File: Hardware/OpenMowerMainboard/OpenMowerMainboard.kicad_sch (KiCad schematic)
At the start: 9 parts, among them U1 LM2596S_MODULE

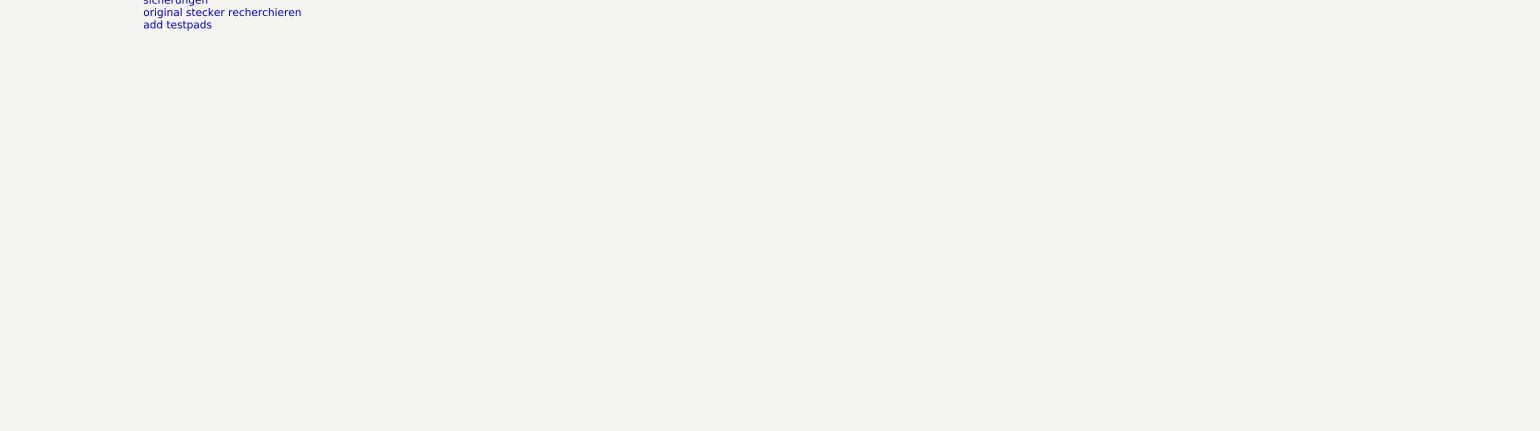
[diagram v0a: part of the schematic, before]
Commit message: added todos, added image of current mainboard
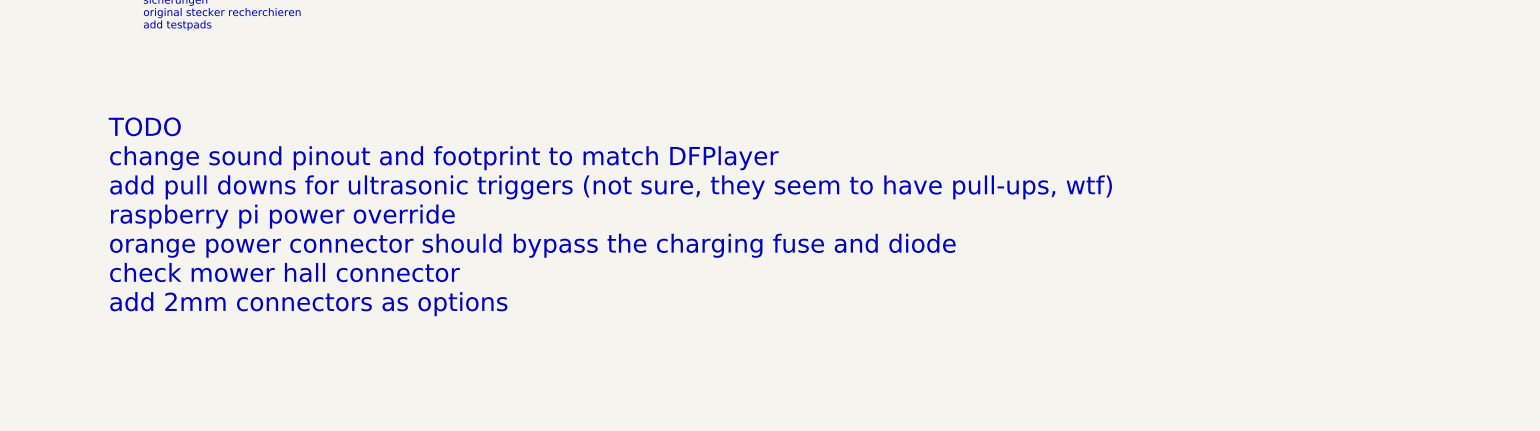
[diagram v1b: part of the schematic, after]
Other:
- note added: "TODO change sound pinout and footprint to match DFPlayer add pull downs for ultrasonic triggers (not sure, they seem to have pull-ups, wtf) raspberry pi power override orange power connector should bypass the charging fuse and diode check mower hall connector add 2mm connectors as options"
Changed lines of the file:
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@@
     (stroke (width 0) (type default) (color 0 0 0 0))
+  )
+  (text "TODO\nchange sound pinout and footprint to match DFPlayer\nadd pull downs for ultrasonic triggers (not sure, they seem to have pull-ups, wtf)\nraspberry pi power override\norange power connector should bypass the charging fuse and diode\ncheck mower hall connector\nadd 2mm connectors as options"
+    (at 282.575 113.665 0)
+    (effects (font (size 3 3)) (justify left bottom))
   )
   (text "Sensor Connectors" (at 50.165 166.37 0)

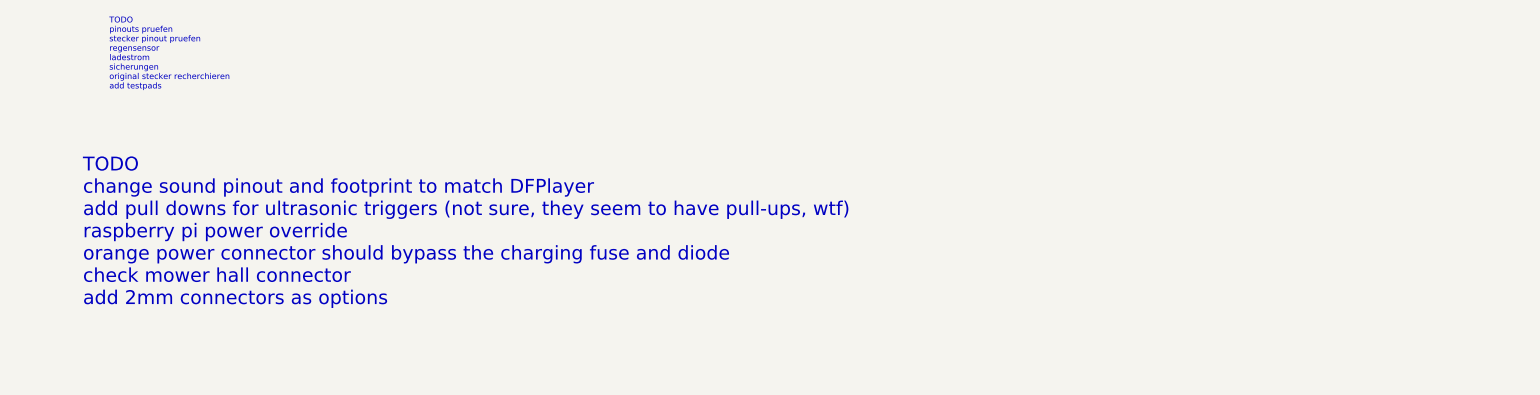
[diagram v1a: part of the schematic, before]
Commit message: Added default pull down, raspberry pi power override and some TODOs
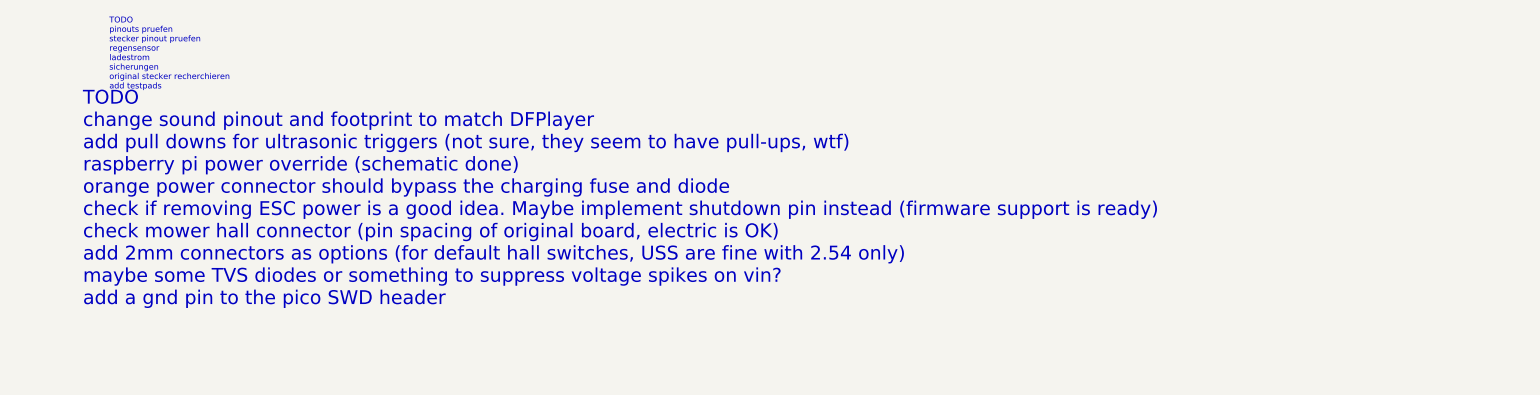
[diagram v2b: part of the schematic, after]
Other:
- note added: "TODO change sound pinout and footprint to match DFPlayer add pull downs for ultrasonic triggers (not sure, they seem to have pull-ups, wtf) raspberry pi power override (schematic done) orange power connector should bypass the charging fuse and diode check if removing ESC power is a good idea. Maybe implement shutdown pin instead (firmware support is ready) check mower hall connector (pin spacing 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"
- note removed: "TODO change sound pinout and footprint to match DFPlayer add pull downs for ultrasonic triggers (not sure, they seem to have pull-ups, wtf) raspberry pi power override orange power connector should bypass the charging fuse and diode check mower hall connector add 2mm connectors as options"
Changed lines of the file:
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@@
     (stroke (width 0) (type default) (color 0 0 0 0))
   )
-  (text "TODO\nchange sound pinout and footprint to match DFPlayer\nadd pull downs for ultrasonic triggers (not sure, they seem to have pull-ups, wtf)\nraspberry pi power override\norange power connector should bypass the charging fuse and diode\ncheck mower hall connector\nadd 2mm connectors as options"
+  (text "TODO\nchange sound pinout and footprint to match DFPlayer\nadd pull downs for ultrasonic triggers (not sure, they seem to have pull-ups, wtf)\nraspberry pi power override (schematic done)\norange power connector should bypass the charging fuse and diode\ncheck if removing ESC power is a good idea. Maybe implement shutdown pin instead (firmware support is ready)\ncheck mower hall connector (pin spacing of original board, electric is OK)\nadd 2mm connectors as options (for default hall switches, USS are fine with 2.54 only)\nmaybe some TVS diodes or something to suppress voltage spikes on vin?\nadd a gnd pin to the pico SWD header"
     (at 282.575 113.665 0)
     (effects (font (size 3 3)) (justify left bottom))
@@
       (reference "R51") (unit 1) (value "R") (footprint "Resistor_SMD:R_2512_6332Metric_Pad1.40x3.35mm_HandSolder")
     )
+    (path "/00000000-0000-0000-0000-00006109dce5/1e0378df-4eb5-4433-998b-5f346ec4a88e"
+      (reference "R?") (unit 1) (value "10k") (footprint "Resistor_SMD:R_0805_2012Metric_Pad1.20x1.40mm_HandSolder")
+    )
+    (path "/00000000-0000-0000-0000-000061080954/524cc440-f69b-4e5c-95c8-45fc44a5eb8a"
+      (reference "R?") (unit 1) (value "10k") (footprint "Resistor_SMD:R_0805_2012Metric_Pad1.20x1.40mm_HandSolder")
+    )
+    (path "/00000000-0000-0000-0000-000061080954/faeb18f8-c222-4c98-a19d-ced7efa28a99"
+      (reference "R?") (unit 1) (value "10k") (footprint "Resistor_SMD:R_0805_2012Metric_Pad1.20x1.40mm_HandSolder")
+    )
     (path "/989a400d-9ce2-403e-a19e-ad0a758fe27c/88528529-64b3-4d79-b2db-e04c4b468443"

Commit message: WIP hardware revision
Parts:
- removed U1: LM2596S_MODULE, MyModules:LM2596S_MODULE, symbol MyModules:LM2596S_MODULE
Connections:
- net V_BATT renamed RobotConnectors/V_BATTERY
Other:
- added sheet dcdc (dcdc.kicad_sch)
- sheet ESCs ports: added none; removed MC_POWER, ML_POWER, MR_POWER
- sheet GPS ports: added none; removed POWER_EN
- sheet RobotConnectors ports: added Enable_Charge, V_BATTERY; removed none
- sheet pico ports: added ENABLE_CHARGE; removed ESC_POWER, GPS_POWER
- note removed: "TODO change sound pinout and footprint to match DFPlayer add pull downs for ultrasonic triggers (not sure, they seem to have pull-ups, wtf) raspberry pi power override (schematic done) orange power connector should bypass the charging fuse and diode check if removing ESC power is a good idea. Maybe implement shutdown pin instead (firmware support is ready) check mower hall connector (pin spacing 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"
- note removed: "TODO pinouts pruefen stecker pinout pruefen regensensor ladestrom sicherungen original stecker recherchieren add testpads"

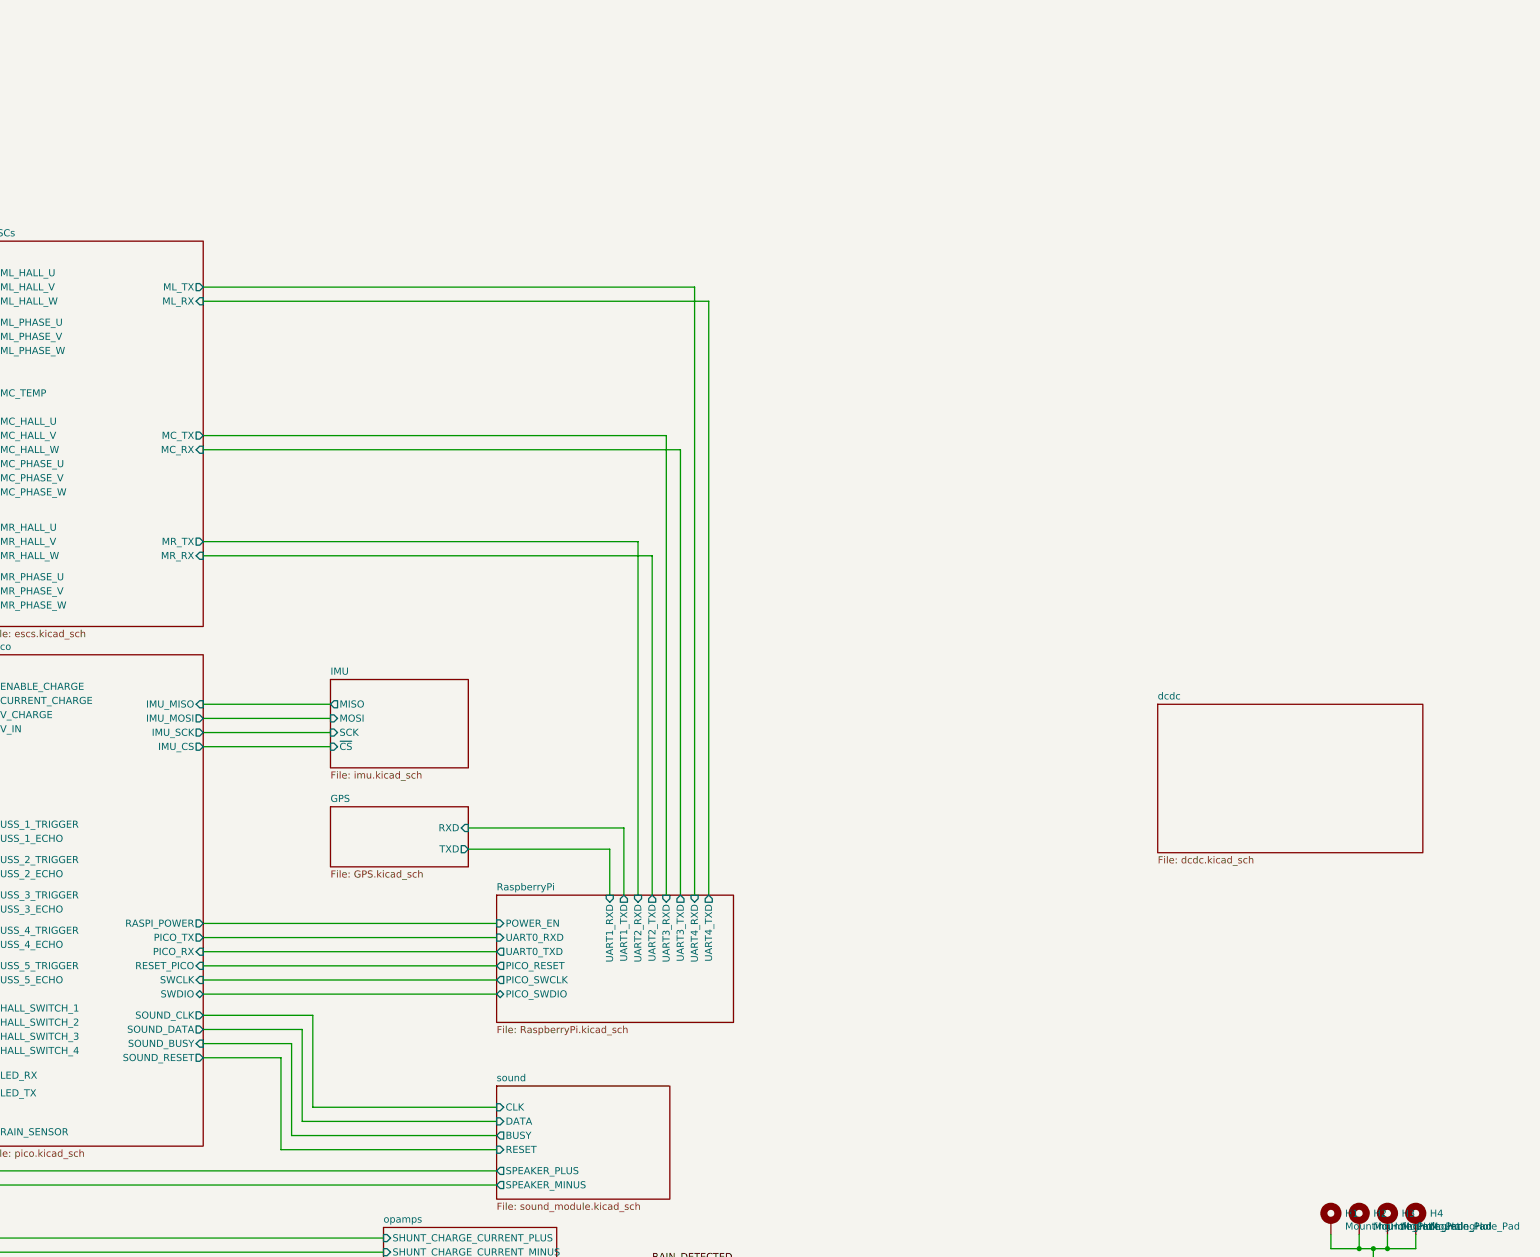
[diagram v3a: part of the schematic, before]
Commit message: v0_9_1 mainboard rework
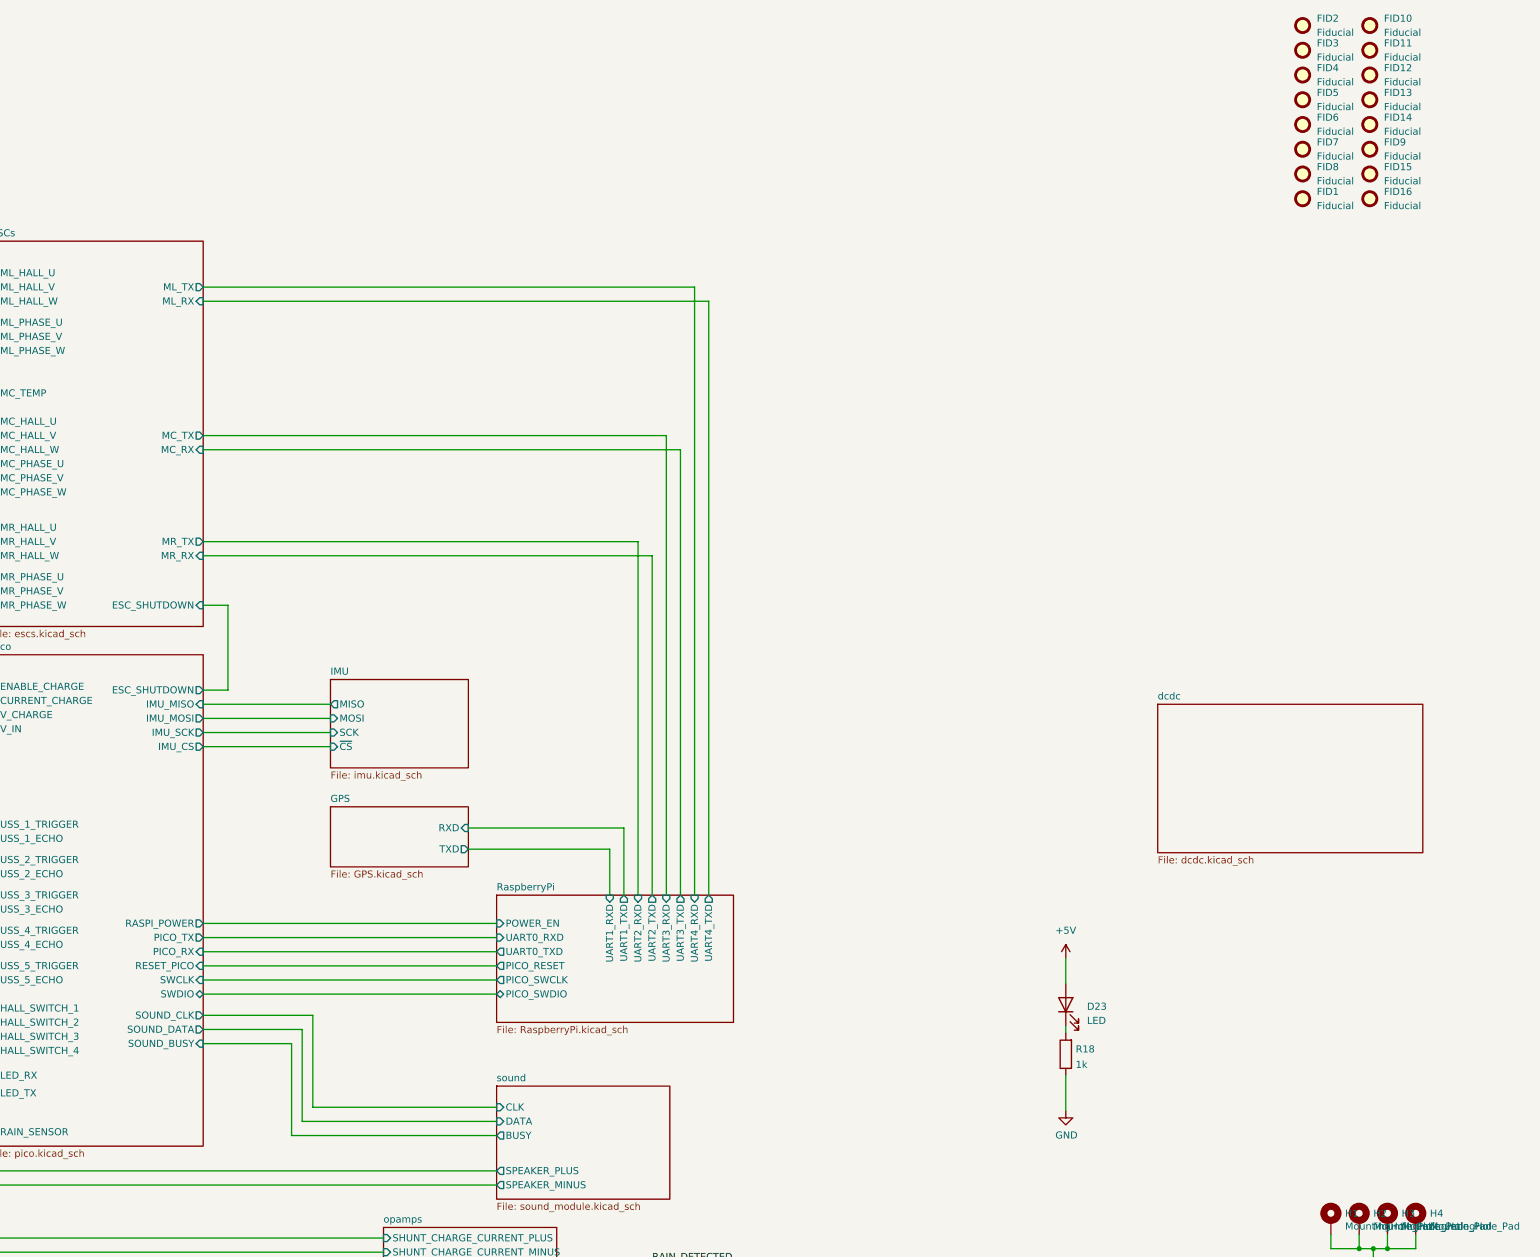
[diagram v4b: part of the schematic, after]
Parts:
- added D23: LED, LED_SMD:LED_0805_2012Metric, symbol Device:LED
- added FID1, FID10, FID11, FID12, FID13, FID14, FID15, FID16, FID2, FID3, FID4, FID5, FID6, FID7, FID8, FID9: Fiducial, Fiducial:Fiducial_1mm_Mask2mm, symbol Mechanical:Fiducial
- added R18: 1k, Resistor_SMD:R_0805_2012Metric_Pad1.20x1.40mm_HandSolder, symbol Device:R
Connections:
- net +5V: now also D23.2 (A)
- net GND: now also R18.1
- new net: D23.1 (K), R18.2
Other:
- sheet ESCs ports: added ESC_SHUTDOWN; removed none
- sheet pico ports: added ESC_SHUTDOWN; removed SOUND_RESET
- sheet sound ports: added none; removed RESET

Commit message: small PCB changes
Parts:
- H1, H2, H3, H4: footprint MountingHole:MountingHole_5mm_Pad -> MountingHole:MountingHole_5mm_Pad_Via
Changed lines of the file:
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@@
       (effects (font (size 1.27 1.27)) (justify left))
     )
-    (property "Footprint" "MountingHole:MountingHole_5mm_Pad" (id 2) (at 373.38 240.03 0)
+    (property "Footprint" "MountingHole:MountingHole_5mm_Pad_Via" (id 2) (at 373.38 240.03 0)
       (effects (font (size 1.27 1.27)) hide)
     )
@@
       (effects (font (size 1.27 1.27)) (justify left))
     )
-    (property "Footprint" "MountingHole:MountingHole_5mm_Pad" (id 2) (at 378.46 240.03 0)
+    (property "Footprint" "MountingHole:MountingHole_5mm_Pad_Via" (id 2) (at 378.46 240.03 0)
       (effects (font (size 1.27 1.27)) hide)
     )
@@
       (effects (font (size 1.27 1.27)) (justify left))
     )
-    (property "Footprint" "MountingHole:MountingHole_5mm_Pad" (id 2) (at 383.54 240.03 0)
+    (property "Footprint" "MountingHole:MountingHole_5mm_Pad_Via" (id 2) (at 383.54 240.03 0)
       (effects (font (size 1.27 1.27)) hide)
     )
@@
       (effects (font (size 1.27 1.27)) (justify left))
     )
-    (property "Footprint" "MountingHole:MountingHole_5mm_Pad" (id 2) (at 388.62 240.03 0)
+    (property "Footprint" "MountingHole:MountingHole_5mm_Pad_Via" (id 2) (at 388.62 240.03 0)
       (effects (font (size 1.27 1.27)) hide)
     )
@@
     )
     (path "/00000000-0000-0000-0000-000060ffea54"
-      (reference "H1") (unit 1) (value "MountingHole_Pad") (footprint "MountingHole:MountingHole_5mm_Pad")
+      (reference "H1") (unit 1) (value "MountingHole_Pad") (footprint "MountingHole:MountingHole_5mm_Pad_Via")
     )
     (path "/00000000-0000-0000-0000-000060fff53b"
-      (reference "H2") (unit 1) (value "MountingHole_Pad") (footprint "MountingHole:MountingHole_5mm_Pad")
+      (reference "H2") (unit 1) (value "MountingHole_Pad") (footprint "MountingHole:MountingHole_5mm_Pad_Via")
     )
     (path "/00000000-0000-0000-0000-000060fff6e7"
-      (reference "H3") (unit 1) (value "MountingHole_Pad") (footprint "MountingHole:MountingHole_5mm_Pad")
+      (reference "H3") (unit 1) (value "MountingHole_Pad") (footprint "MountingHole:MountingHole_5mm_Pad_Via")
     )
     (path "/00000000-0000-0000-0000-000060fff86d"
-      (reference "H4") (unit 1) (value "MountingHole_Pad") (footprint "MountingHole:MountingHole_5mm_Pad")
+      (reference "H4") (unit 1) (value "MountingHole_Pad") (footprint "MountingHole:MountingHole_5mm_Pad_Via")
     )
     (path "/00000000-0000-0000-0000-000061040c60/487d2bd1-f483-496f-9e00-2a685e78df55"

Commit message: BoM data added to kicad - results exported to .xlsx file
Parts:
- D23: Digikey (none) -> L62505CT-ND; Part Number (none) -> CMD17-21VGD/TR8; Stock_PN (none) -> LED-805-GREEN
- FID1, FID10, FID11, FID12, FID13, FID14, FID15, FID16, FID2, FID3, FID4, FID5, FID6, FID7, FID8, FID9, H1, H2, H3, H4: Config (none) -> do not place
- R18, R41, R43: Digikey (none) -> 311-1.00KCRCT-ND; Part Number (none) -> RC0805FR-071KL; Stock_PN (none) -> R-805-1K-.125W-1%
- R40, R42: Digikey (none) -> 738-RMCF0805FG10K0CT-ND; Part Number (none) -> RMCF0805FG10K0; Stock_PN (none) -> R-805-10K-.125W-1%
